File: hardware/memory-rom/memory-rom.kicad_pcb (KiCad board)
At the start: 2 copper layers, 77 x 39 mm, 26 parts, among them J1 Conn_Mem_Ext, J2 Conn_Power, U1 SST39VF040-70-4C-NHE, U2 74LVC1G86, U3 74LVC1G32, U4 74LVC1G332, U5 74LVC1G86, U6 MIC5504-3.3YM5

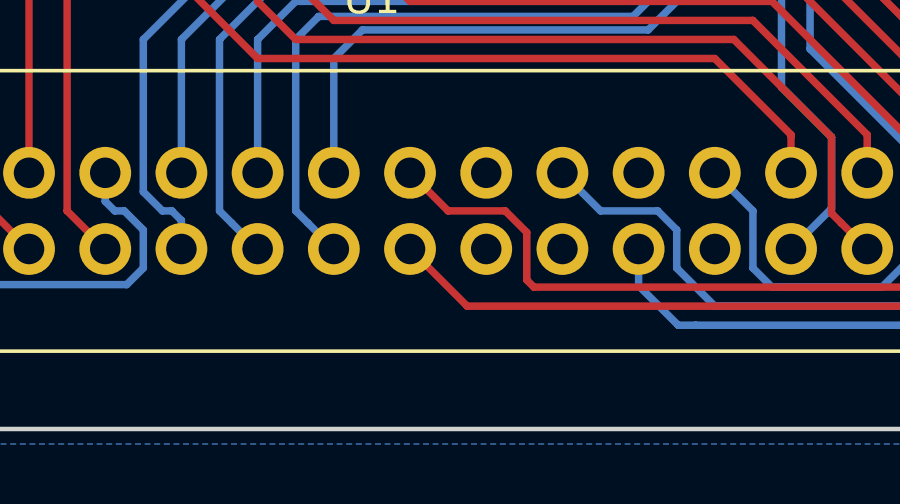
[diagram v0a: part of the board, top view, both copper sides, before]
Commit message: Added placeholders for JLCPCB serial numbers
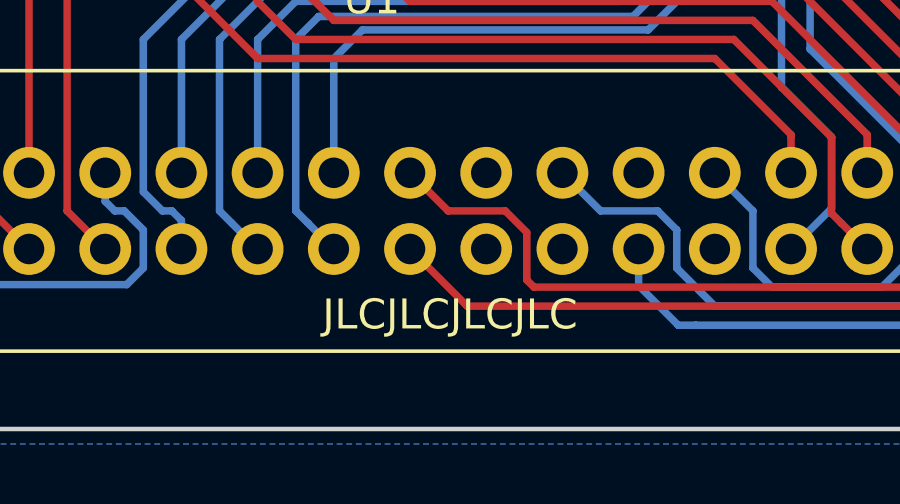
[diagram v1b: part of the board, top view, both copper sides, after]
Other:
- board text added: "JLCJLCJLCJLC"
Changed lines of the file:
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@@
   (general
     (thickness 1.6)
-    (drawings 15)
+    (drawings 16)
     (tracks 550)
     (zones 0)
@@
     )
   )
+  (gr_text JLCJLCJLCJLC (at 104.08 129.185) (layer F.SilkS)
+    (effects (font (size 1 1) (thickness 0.15)))
+  )
   (gr_text GND (at 136.75 120) (layer B.SilkS)
